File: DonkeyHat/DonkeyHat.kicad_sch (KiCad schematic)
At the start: 14 parts, among them J1 GPIO, J2 Encoder 2, J3 Encoder 1, J4 I2C, J5 Conn_02x03_Odd_Even, J6 Conn_02x03_Odd_Even, U2 rp2040-zero

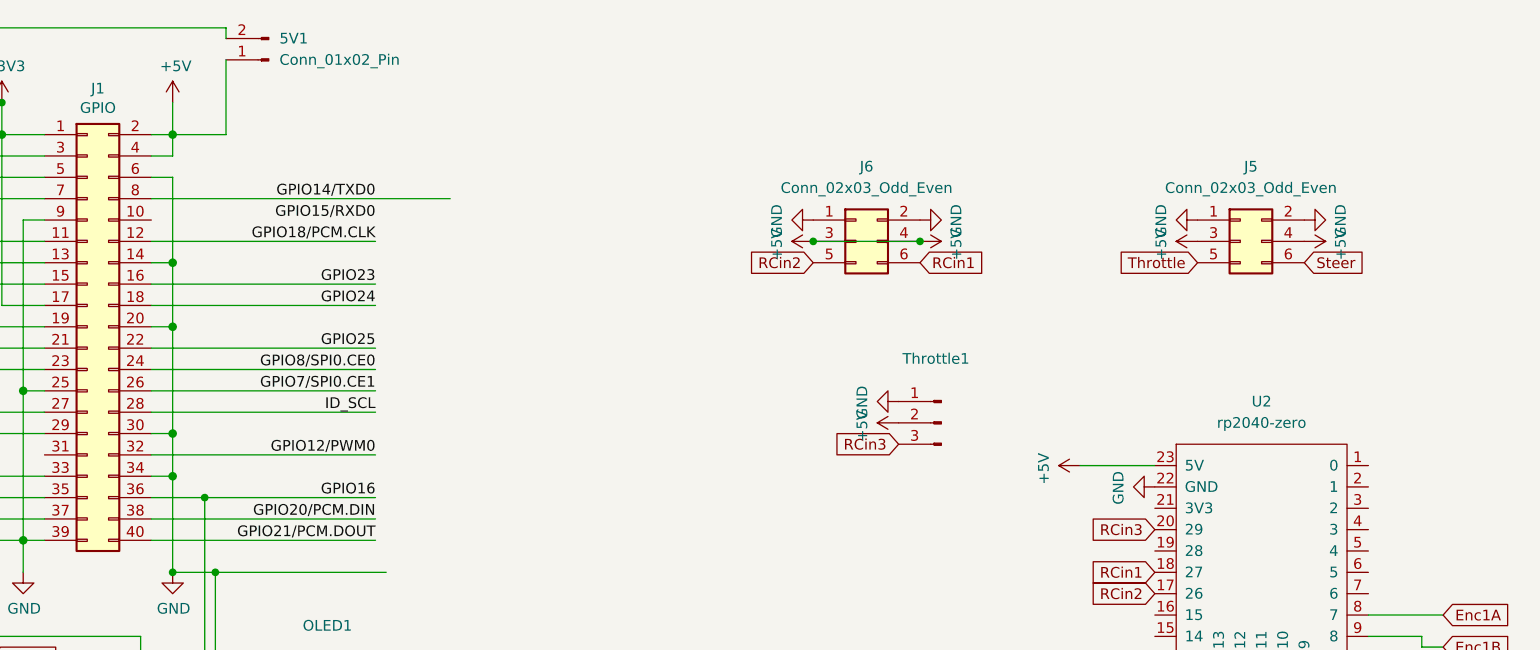
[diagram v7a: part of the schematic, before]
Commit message: Battery power for servos
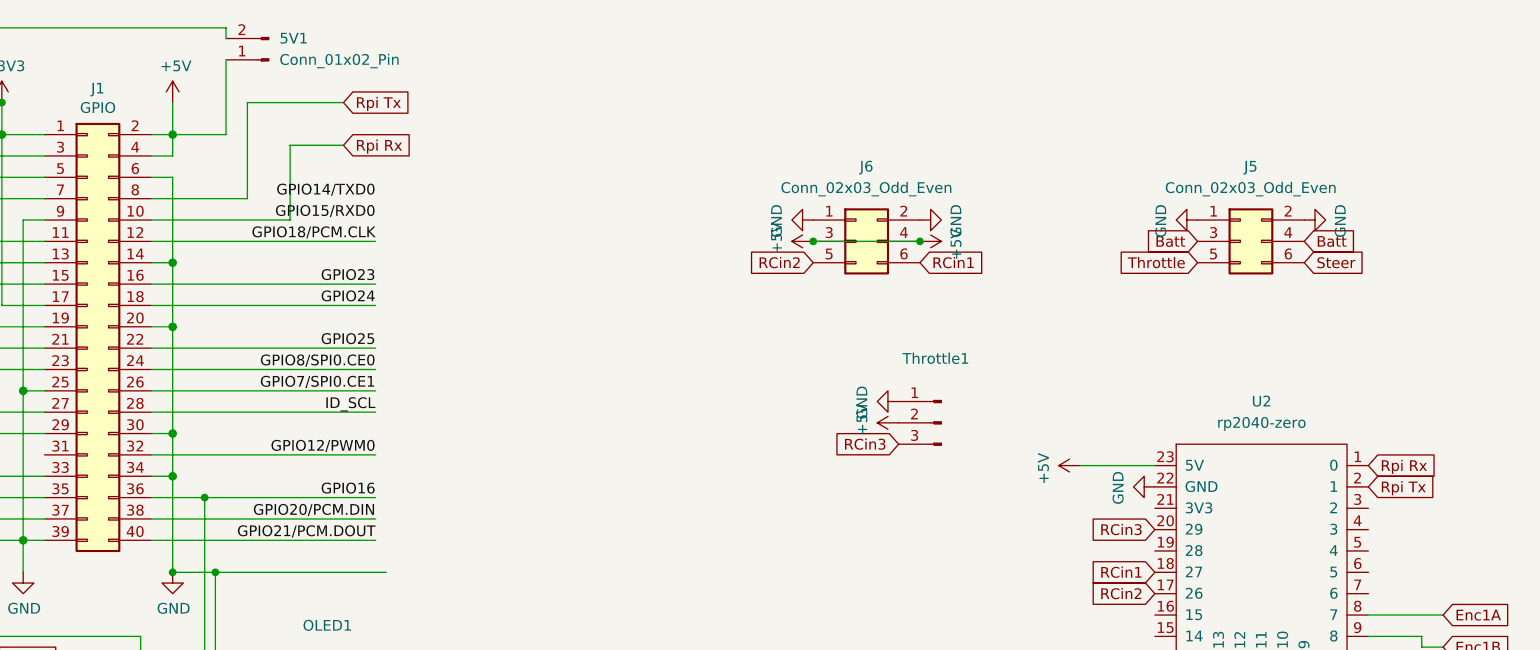
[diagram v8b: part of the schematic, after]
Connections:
- net +5V: no longer J5.3 (Pin_3), J5.4 (Pin_4)
- net GPIO14/TXD0: no longer J1.8 (Pin_8)
- net Rpi Rx: now reaches J1.10 (Pin_10)
- net Rpi Rx: now also U2.1 (0)
- net Rpi Tx: now reaches U2.2 (1)
- net Rpi Tx: now also J1.8 (Pin_8)
- new net Batt: J5.3 (Pin_3), J5.4 (Pin_4)
